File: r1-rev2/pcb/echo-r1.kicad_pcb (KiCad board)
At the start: 6 copper layers, 140 x 120.6 mm, 152 parts, among them J1 TYPE-C-31-M-12, J2 TF-115, J3 HP_3.5mm, J4 LO_3.5mm, J5 GT-BTP30003-xxxA-16A, J6 AFC07-S30ECA-00, J7 Conn_SWDUART, J9 Micro_SD_Card, Q1 AO3401A, Q2 AO3401A, Q3 AO3401A, Q4 AO3401A, Q5 AO3401A, SW1 A, SW10 SELECT, SW11 VOL+, SW12 VOL-, SW13 POWER, SW14 HOLD, SW2 B, SW3 X, SW4 Y, SW5 DPAD↑, SW6 DPAD↓, SW7 DPAD←, SW8 DPAD→, SW9 START, U1 STM32H7R3Z8Jx, U10 USBLC6-2SC6, U11 TPAZ1143-04F, U12 TPAZ1143-04F, U13 TPAZ1143-04F, U14 TPAZ1143-04F, U15 TPAZ1143-04F, U16 TPAZ1143-04F, U2 W958D8NBYA5I, U3 TLV320AIC3104, U4 LM66100DCK, U5 TPS62A01DRLR, U6 TPS62A01DRLR, U7 AP2125K-3.0, U8 AP2125K-3.0, U9 TP4057, Y1 SC-32S32.768kHz20PPM12.5pF, Y2 XTM32024000JT00351001

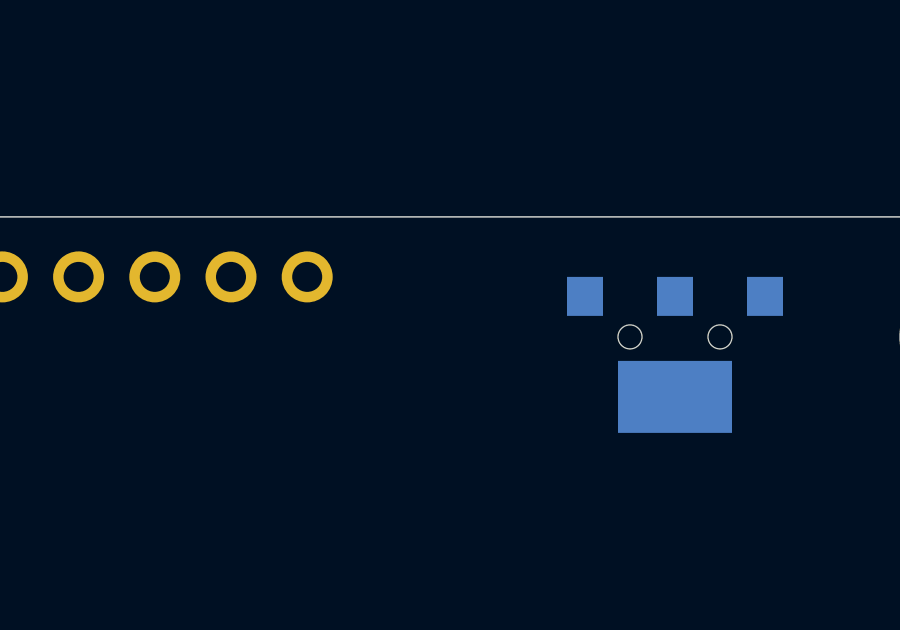
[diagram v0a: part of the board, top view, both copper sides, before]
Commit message: R1-Rev2: add optional connection point for a wired battery
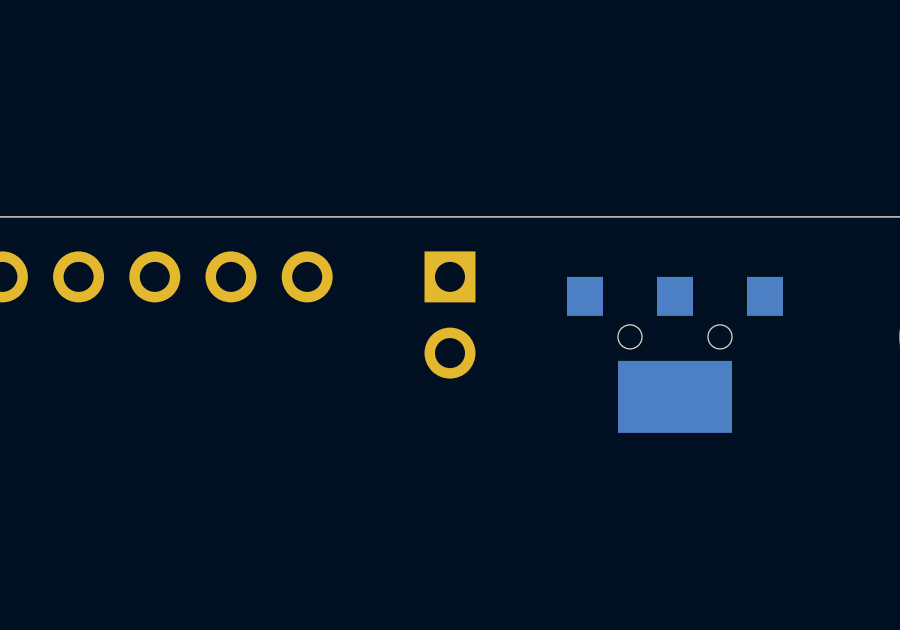
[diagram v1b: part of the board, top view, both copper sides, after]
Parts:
- added J8: Conn_01x02, Connector_PinHeader_2.54mm:PinHeader_1x02_P2.54mm_Vertical, B.Cu at (152.5, 60.0)
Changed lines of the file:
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@@
+		)
+	)
+	(footprint "Connector_PinHeader_2.54mm:PinHeader_1x02_P2.54mm_Vertical"
+		(locked yes)
+		(layer "B.Cu")
+		(at 152.5 60 180)
+		(descr "Through hole straight pin header, 1x02, 2.54mm pitch, single row")
+		(tags "Through hole pin header THT 1x02 2.54mm single row")
+		(property "Reference" "J8"
+			(at 0 2.33 0)
+			(layer "B.SilkS")
+			(effects
+				(font
+					(size 1 1)
+					(thickness 0.15)
+				)
+				(justify mirror)
+			)
+		)
+		(property "Value" "Conn_01x02"
+			(at 0 -4.87 0)
+			(layer "B.Fab")
+			(effects
+				(font
+					(size 1 1)
+					(thickness 0.15)
+				)
+				(justify mirror)
+			)
+		)
+		(property "Datasheet" ""
+			(at 0 0 0)
+			(unlocked yes)
+			(layer "B.Fab")
+			(hide yes)
+			(effects
+				(font
+					(size 1.27 1.27)
+					(thickness 0.15)
+				)
+				(justify mirror)
+			)
+		)
+		(property "Description" "Generic connector, single row, 01x02, script generated (kicad-library-utils/schlib/autogen/connector/)"
+			(at 0 0 0)
+			(unlocked yes)
+			(layer "B.Fab")
+			(hide yes)
+			(effects
+				(font
+					(size 1.27 1.27)
+					(thickness 0.15)
+				)
+				(justify mirror)
+			)
+		)
+		(property ki_fp_filters "Connector*:*_1x??_*")
+		(sheetname "/power/")
+		(sheetfile "power_supply.kicad_sch")
+		(attr through_hole)
+		(fp_line
+			(start 1.33 -1.27)
+			(end 1.33 -3.87)
+			(stroke
+				(width 0.12)
+				(type solid)
+			)
+			(layer "B.SilkS")
+		)
+		(fp_line
+			(start -1.33 1.33)
+			(end 0 1.33)
+			(stroke
+				(width 0.12)
+				(type solid)
+			)
+			(layer "B.SilkS")
+		)
+		(fp_line
+			(start -1.33 0)
+			(end -1.33 1.33)
+			(stroke
+				(width 0.12)
+				(type solid)
+			)
+			(layer "B.SilkS")
+		)
+		(fp_line
+			(start -1.33 -1.27)
+			(end 1.33 -1.27)
+			(stroke
+				(width 0.12)
+				(type solid)
+			)
+			(layer "B.SilkS")
+		)
+		(fp_line
+			(start -1.33 -1.27)
+			(end -1.33 -3.87)
+			(stroke
+				(width 0.12)
+				(type solid)
+			)
+			(layer "B.SilkS")
+		)
+		(fp_line
+			(start -1.33 -3.87)
+			(end 1.33 -3.87)
+			(stroke
+				(width 0.12)
+				(type solid)
+			)
+			(layer "B.SilkS")
+		)
+		(fp_line
+			(start 1.8 1.8)
+			(end -1.8 1.8)
+			(stroke
+				(width 0.05)
+				(type solid)
+			)
+			(layer "B.CrtYd")
+		)
+		(fp_line
+			(start 1.8 -4.35)
+			(end 1.8 1.8)
+			(stroke
+				(width 0.05)
+				(type solid)
+			)
+			(layer "B.CrtYd")
+		)
+		(fp_line
+			(start -1.8 1.8)
+			(end -1.8 -4.35)
+			(stroke
+				(width 0.05)
+				(type solid)
+			)
+			(layer "B.CrtYd")
+		)
+		(fp_line
+			(start -1.8 -4.35)
+			(end 1.8 -4.35)
+			(stroke
+				(width 0.05)
+				(type solid)
+			)
+			(layer "B.CrtYd")
+		)
+		(fp_line
+			(start 1.27 1.27)
+			(end 1.27 -3.81)
+			(stroke
+				(width 0.1)
+				(type solid)
+			)
+			(layer "B.Fab")
+		)
+		(fp_line
+			(start 1.27 -3.81)
+			(end -1.27 -3.81)
+			(stroke
+				(width 0.1)
+				(type solid)
+			)
+			(layer "B.Fab")
+		)
+		(fp_line
+			(start -0.635 1.27)
+			(end 1.27 1.27)
+			(stroke
+				(width 0.1)
+				(type solid)
+			)
+			(layer "B.Fab")
+		)
+		(fp_line
+			(start -1.27 0.635)
+			(end -0.635 1.27)
+			(stroke
+				(width 0.1)
+				(type solid)
+			)
+			(layer "B.Fab")
+		)
+		(fp_line
+			(start -1.27 -3.81)
+			(end -1.27 0.635)
+			(stroke
+				(width 0.1)
+				(type solid)
+			)
+			(layer "B.Fab")
+		)
+		(fp_text user "${REFERENCE}"
+			(at 0 -1.27 90)
+			(layer "B.Fab")
+			(effects
+				(font
+					(size 1 1)
+					(thickness 0.15)
+				)
+				(justify mirror)
+			)
+		)
+		(pad "1" thru_hole rect
+			(at 0 0 180)
+			(size 1.7 1.7)
+			(drill 1)
+			(layers "*.Cu" "*.Mask")
+			(remove_unused_layers no)
+			(net 151 "VBAT")
+			(pinfunction "Pin_1")
+			(pintype "passive")
+		)
+		(pad "2" thru_hole oval
+			(at 0 -2.54 180)
+			(size 1.7 1.7)
+			(drill 1)
+			(layers "*.Cu" "*.Mask")
+			(remove_unused_layers no)
+			(net 1 "GND")
+			(pinfunction "Pin_2")
+			(pintype "passive")
+		)
+		(embedded_fonts no)
+		(model "${KICAD8_3DMODEL_DIR}/Connector_PinHeader_2.54mm.3dshapes/PinHeader_1x02_P2.54mm_Vertical.wrl"
+			(offset
+				(xyz 0 0 0)
+			)
+			(scale
+				(xyz 1 1 1)
+			)
+			(rotate
+				(xyz 0 0 0)
+			)
 		)
 	)

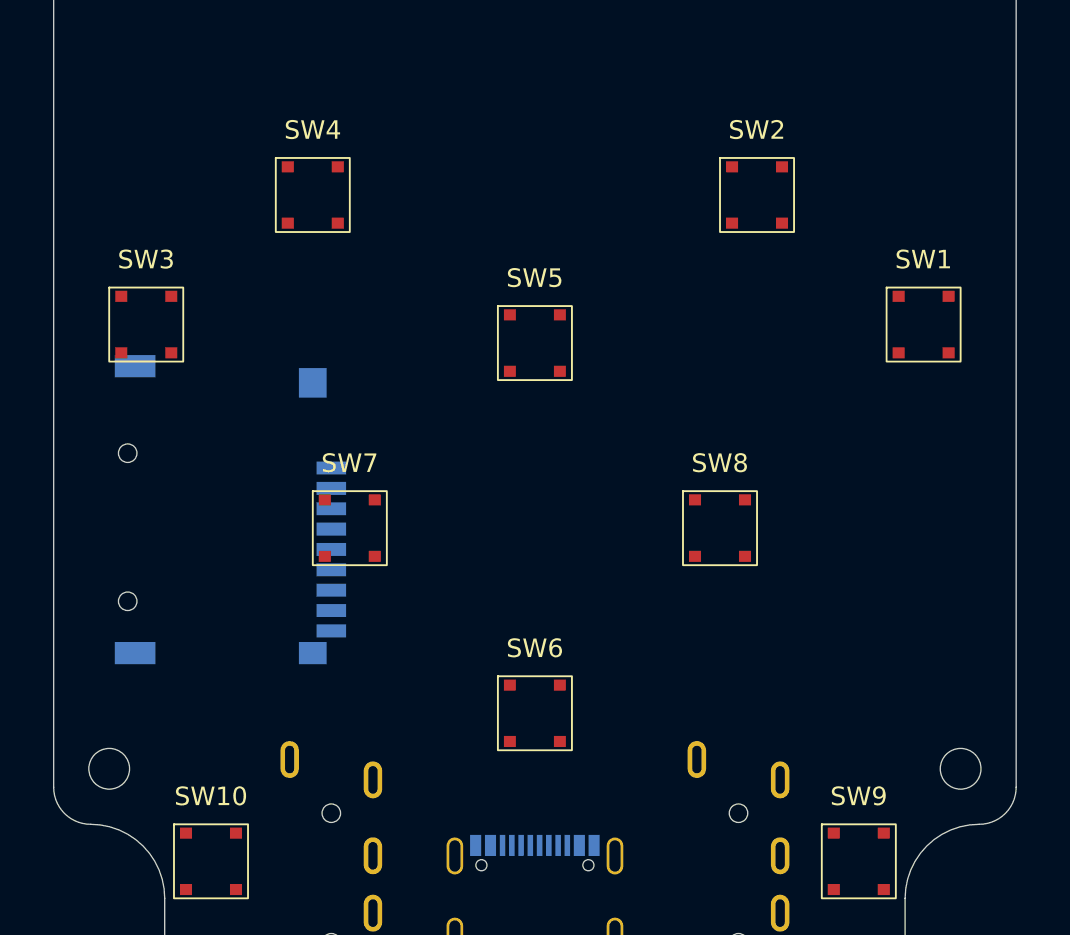
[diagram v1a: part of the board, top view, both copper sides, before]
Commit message: R1-Rev2: fix/improve fab layer text on a few footprints
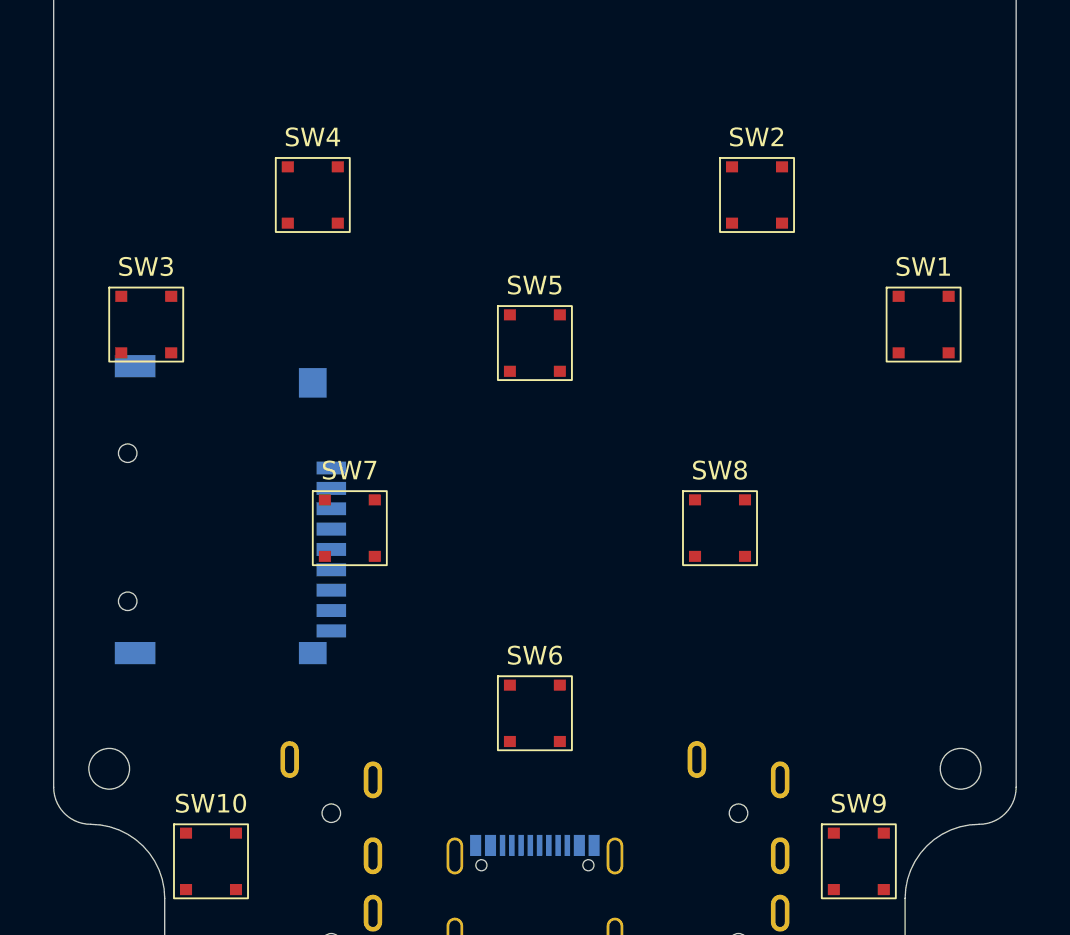
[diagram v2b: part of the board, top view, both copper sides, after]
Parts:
- J8: value Conn_01x02 -> BATT
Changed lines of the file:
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@@
 		(tags "smd dome swich spst")
 		(property "Reference" "SW8"
-			(at 0 -3.5 0)
+			(at 0 -3.1 0)
 			(unlocked yes)
 			(layer "F.SilkS")
@@
 		)
 		(property "Value" "DPAD→"
-			(at 0 3.5 0)
+			(at 0 2.7 0)
 			(unlocked yes)
 			(layer "F.Fab")
@@
 		)
 		(fp_text user "${REFERENCE}"
-			(at 0 5 0)
+			(at 0 -2.7 0)
 			(unlocked yes)
 			(layer "F.Fab")
@@
 		(tags "smd dome swich spst")
 		(property "Reference" "SW1"
-			(at 0 -3.5 0)
+			(at 0 -3.1 0)
 			(unlocked yes)
 			(layer "F.SilkS")
@@
 		)
 		(property "Value" "A"
-			(at 0 3.5 0)
+			(at 0 2.7 0)
 			(unlocked yes)
 			(layer "F.Fab")
@@
 		)
 		(fp_text user "${REFERENCE}"
-			(at 0 5 0)
+			(at 0 -2.7 0)
 			(unlocked yes)
 			(layer "F.Fab")
@@
 		(tags "smd dome swich spst")
 		(property "Reference" "SW5"
-			(at 0 -3.5 0)
+			(at 0 -3.1 0)
 			(unlocked yes)
 			(layer "F.SilkS")
@@
 		)
 		(property "Value" "DPAD↑"
-			(at 0 3.5 0)
+			(at 0 2.7 0)
 			(unlocked yes)
 			(layer "F.Fab")
@@
 		)
 		(fp_text user "${REFERENCE}"
-			(at 0 5 0)
+			(at 0 -2.7 0)
 			(unlocked yes)
 			(layer "F.Fab")
@@
 		(tags "smd dome swich spst")
 		(property "Reference" "SW2"
-			(at 0 -3.5 0)
+			(at 0 -3.1 0)
 			(unlocked yes)
 			(layer "F.SilkS")
@@
 		)
 		(property "Value" "B"
-			(at 0 3.5 0)
+			(at 0 2.7 0)
 			(unlocked yes)
 			(layer "F.Fab")
@@
 		)
 		(fp_text user "${REFERENCE}"
-			(at 0 5 0)
+			(at 0 -2.7 0)
 			(unlocked yes)
 			(layer "F.Fab")
@@
 		(tags "smd dome swich spst")
 		(property "Reference" "SW10"
-			(at 0 -3.5 0)
+			(at 0 -3.1 0)
 			(unlocked yes)
 			(layer "F.SilkS")
@@
 		)
 		(property "Value" "SELECT"
-			(at 0 3.5 0)
+			(at 0 2.7 0)
 			(unlocked yes)
 			(layer "F.Fab")
@@
 		)
 		(fp_text user "${REFERENCE}"
-			(at 0 5 0)
+			(at 0 -2.7 0)
 			(unlocked yes)
 			(layer "F.Fab")
@@
 		(tags "smd dome swich spst")
 		(property "Reference" "SW6"
-			(at 0 -3.5 0)
+			(at 0 -3.1 0)
 			(unlocked yes)
 			(layer "F.SilkS")
@@
 		)
 		(property "Value" "DPAD↓"
-			(at 0 3.5 0)
+			(at 0 2.7 0)
 			(unlocked yes)
 			(layer "F.Fab")
@@
 		)
 		(fp_text user "${REFERENCE}"
-			(at 0 5 0)
+			(at 0 -2.7 0)
 			(unlocked yes)
 			(layer "F.Fab")
@@
 		(tags "smd dome swich spst")
 		(property "Reference" "SW7"
-			(at 0 -3.5 0)
+			(at 0 -3.1 0)
 			(unlocked yes)
 			(layer "F.SilkS")
@@
 		)
 		(property "Value" "DPAD←"
-			(at 0 3.5 0)
+			(at 0 2.7 0)
 			(unlocked yes)
 			(layer "F.Fab")
@@
 		)
 		(fp_text user "${REFERENCE}"
-			(at 0 5 0)
+			(at 0 -2.7 0)
 			(unlocked yes)
 			(layer "F.Fab")
@@
 		(tags "smd dome swich spst")
 		(property "Reference" "SW3"
-			(at 0 -3.5 0)
+			(at 0 -3.1 0)
 			(unlocked yes)
 			(layer "F.SilkS")
@@
 		)
 		(property "Value" "X"
-			(at 0 3.5 0)
+			(at 0 2.7 0)
 			(unlocked yes)
 			(layer "F.Fab")
@@
 		)
 		(fp_text user "${REFERENCE}"
-			(at 0 5 0)
+			(at 0 -2.7 0)
 			(unlocked yes)
 			(layer "F.Fab")
@@
 		(tags "smd dome swich spst")
 		(property "Reference" "SW9"
-			(at 0 -3.5 0)
+			(at 0 -3.1 0)
 			(unlocked yes)
 			(layer "F.SilkS")
@@
 		)
 		(property "Value" "START"
-			(at 0 3.5 0)
+			(at 0 2.7 0)
 			(unlocked yes)
 			(layer "F.Fab")
@@
 		)
 		(fp_text user "${REFERENCE}"
-			(at 0 5 0)
+			(at 0 -2.7 0)
 			(unlocked yes)
 			(layer "F.Fab")
@@
 		(tags "smd dome swich spst")
 		(property "Reference" "SW4"
-			(at 0 -3.5 0)
+			(at 0 -3.1 0)
 			(unlocked yes)
 			(layer "F.SilkS")
@@
 		)
 		(property "Value" "Y"
-			(at 0 3.5 0)
+			(at 0 2.7 0)
 			(unlocked yes)
 			(layer "F.Fab")
@@
 		)
 		(fp_text user "${REFERENCE}"
-			(at 0 5 0)
+			(at 0 -2.7 0)
 			(unlocked yes)
 			(layer "F.Fab")
@@
 		)
 		(property "Value" "HOLD"
-			(at 0 -3.5 90)
+			(at 0 -2.2 90)
 			(unlocked yes)
 			(layer "B.Fab")
@@
 		)
 		(fp_text user "${REFERENCE}"
-			(at 5 0 0)
+			(at 0 0 90)
 			(unlocked yes)
 			(layer "B.Fab")
@@
 			(size 1.05 0.7)
 			(layers "B.Cu" "B.Mask" "B.Paste")
-			(net 128 "unconnected-(SW14-PadMP)_3")
+			(net 126 "unconnected-(SW14-PadMP)_1")
 			(pinfunction "MP")
 			(pintype "passive+no_connect")
@@
 			(size 1.05 0.7)
 			(layers "B.Cu" "B.Mask" "B.Paste")
-			(net 126 "unconnected-(SW14-PadMP)_1")
+			(net 125 "unconnected-(SW14-PadMP)")
 			(pinfunction "MP")
 			(pintype "passive+no_connect")
@@
 			(size 1.05 0.7)
 			(layers "B.Cu" "B.Mask" "B.Paste")
-			(net 127 "unconnected-(SW14-PadMP)_2")
+			(net 128 "unconnected-(SW14-PadMP)_3")
 			(pinfunction "MP")
 			(pintype "passive+no_connect")
@@
 			(size 1.05 0.7)
 			(layers "B.Cu" "B.Mask" "B.Paste")
-			(net 125 "unconnected-(SW14-PadMP)")
+			(net 127 "unconnected-(SW14-PadMP)_2")
 			(pinfunction "MP")
 			(pintype "passive+no_connect")
@@
 		)
 		(property "Value" "TYPE-C-31-M-12"
-			(at 0 0 0)
+			(at 0 -7.2 0)
 			(layer "B.Fab")
 			(effects
@@
 		)
 		(fp_text user "${REFERENCE}"
-			(at 0 0 0)
+			(at 0 -1.6 0)
 			(layer "B.Fab")
 			(effects
@@
 		)
 		(property "Value" "Conn_SWDUART"
-			(at 0 -17.57 90)
+			(at -2 -8 0)
 			(layer "B.Fab")
 			(effects
@@
 			)
 		)
-		(property "Value" "Conn_01x02"
-			(at 0 -4.87 0)
+		(property "Value" "BATT"
+			(at 2 -1 90)
 			(layer "B.Fab")
 			(effects
